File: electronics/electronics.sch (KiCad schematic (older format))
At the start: 19 parts, among them J3 EXTERNAL CONTROL, J4 POWER, J5 I2C BUS, J6 I2C BUS, J7 INPUT, J8 OUTPUT, U1 ProMicro

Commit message: Last through hole
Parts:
- R5, R6, R7, R8: footprint Resistor_THT:R_Axial_DIN0204_L3.6mm_D1.6mm_P1.90mm_Vertical -> Resistor_THT:R_Axial_DIN0204_L3.6mm_D1.6mm_P2.54mm_Vertical
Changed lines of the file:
@@
 F 0 "R5" H 7068 2346 50  0000 L CNN
 F 1 "75" H 7068 2255 50  0000 L CNN
-F 2 "Resistor_THT:R_Axial_DIN0204_L3.6mm_D1.6mm_P1.90mm_Vertical" H 7000 2300 50  0001 C CNN
+F 2 "Resistor_THT:R_Axial_DIN0204_L3.6mm_D1.6mm_P2.54mm_Vertical" H 7000 2300 50  0001 C CNN
 F 3 "~" H 7000 2300 50  0001 C CNN
 	1    7000 2300
@@
 F 0 "R6" H 7418 2346 50  0000 L CNN
 F 1 "75" H 7418 2255 50  0000 L CNN
-F 2 "Resistor_THT:R_Axial_DIN0204_L3.6mm_D1.6mm_P1.90mm_Vertical" H 7350 2300 50  0001 C CNN
+F 2 "Resistor_THT:R_Axial_DIN0204_L3.6mm_D1.6mm_P2.54mm_Vertical" H 7350 2300 50  0001 C CNN
 F 3 "~" H 7350 2300 50  0001 C CNN
 	1    7350 2300
@@
 F 0 "R7" H 7768 2346 50  0000 L CNN
 F 1 "75" H 7768 2255 50  0000 L CNN
-F 2 "Resistor_THT:R_Axial_DIN0204_L3.6mm_D1.6mm_P1.90mm_Vertical" H 7700 2300 50  0001 C CNN
+F 2 "Resistor_THT:R_Axial_DIN0204_L3.6mm_D1.6mm_P2.54mm_Vertical" H 7700 2300 50  0001 C CNN
 F 3 "~" H 7700 2300 50  0001 C CNN
 	1    7700 2300
@@
 F 0 "R8" H 8068 2346 50  0000 L CNN
 F 1 "75" H 8068 2255 50  0000 L CNN
-F 2 "Resistor_THT:R_Axial_DIN0204_L3.6mm_D1.6mm_P1.90mm_Vertical" H 8000 2300 50  0001 C CNN
+F 2 "Resistor_THT:R_Axial_DIN0204_L3.6mm_D1.6mm_P2.54mm_Vertical" H 8000 2300 50  0001 C CNN
 F 3 "~" H 8000 2300 50  0001 C CNN
 	1    8000 2300

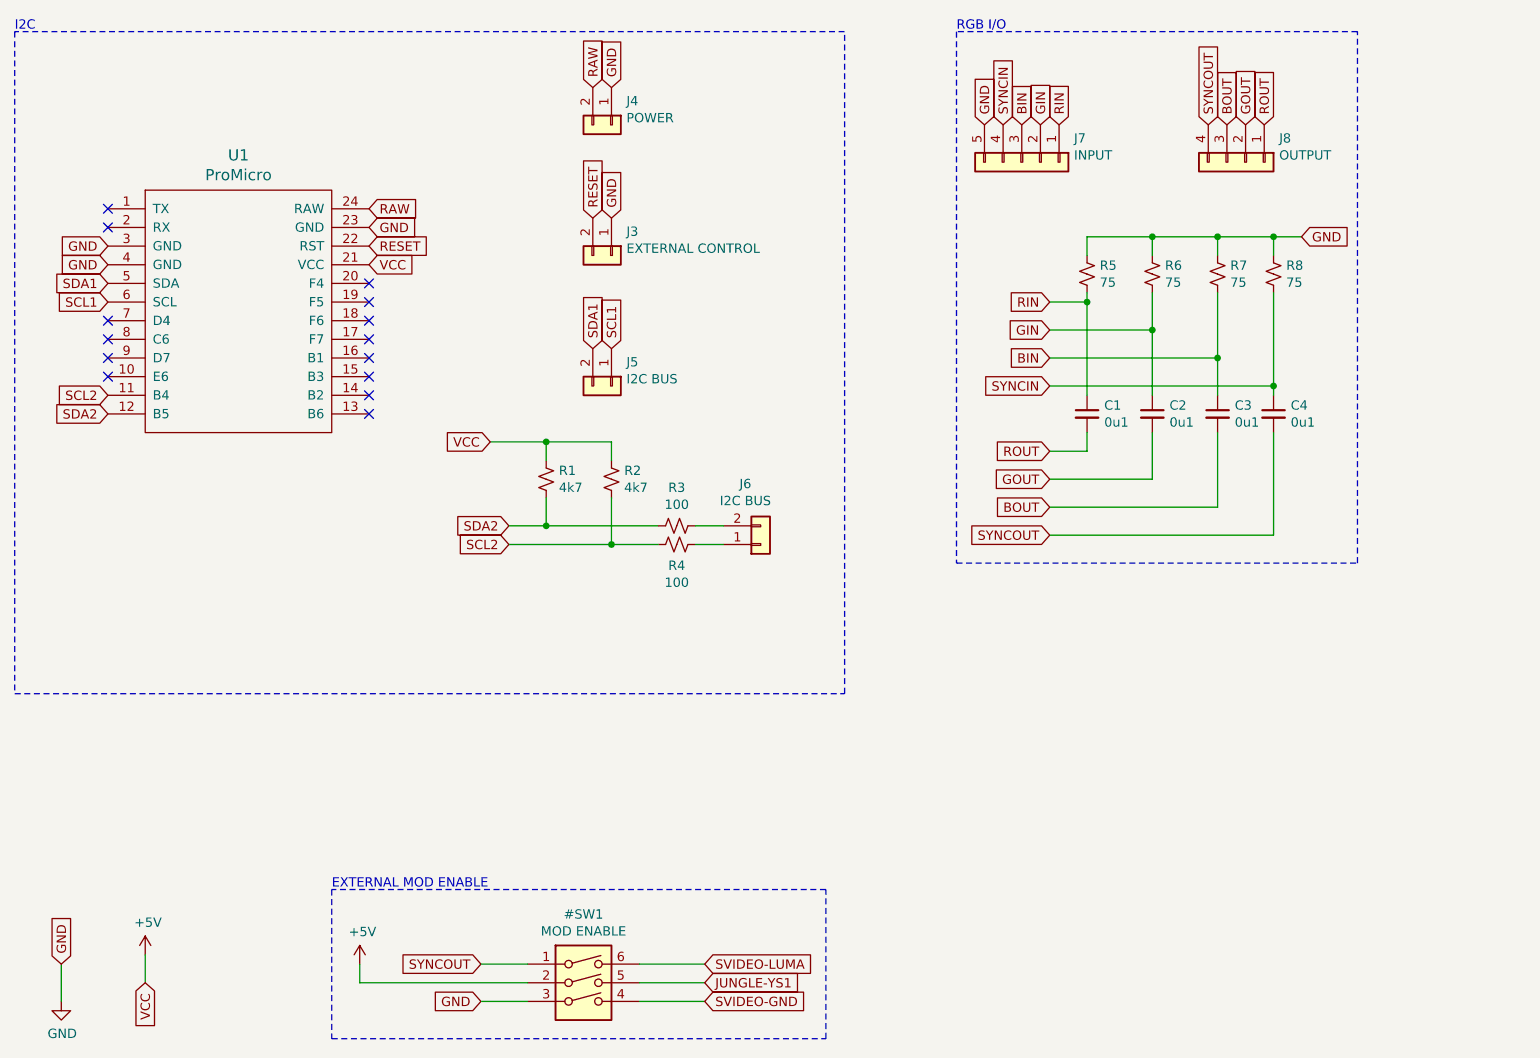
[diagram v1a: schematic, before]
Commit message: Encoder support
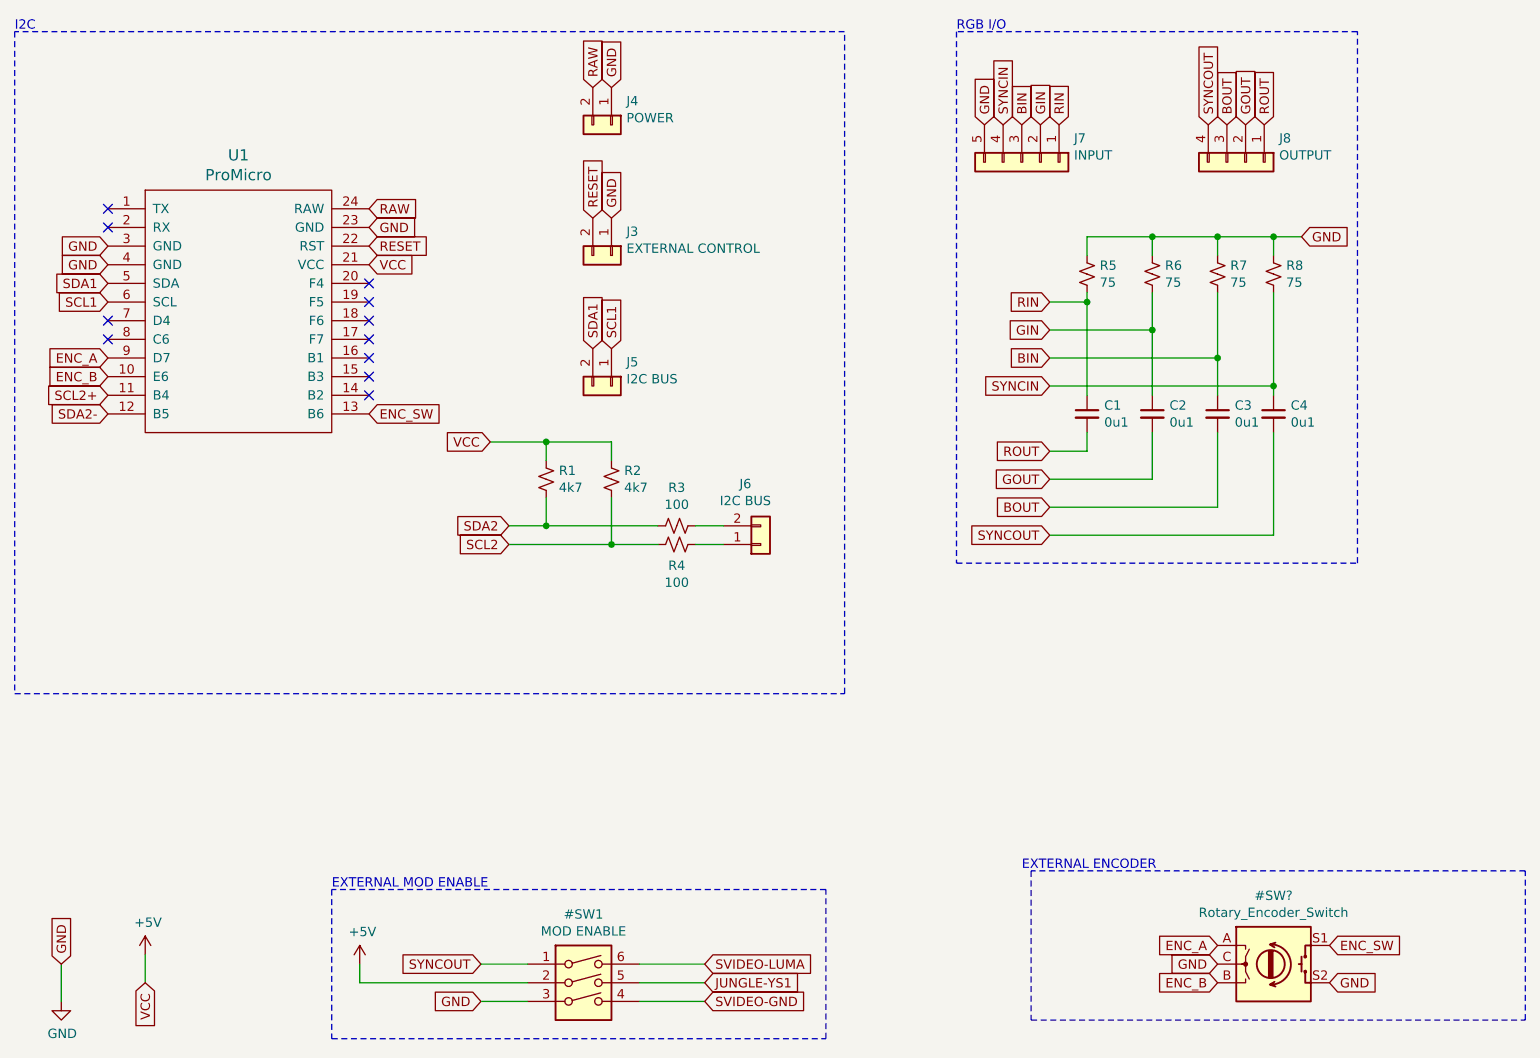
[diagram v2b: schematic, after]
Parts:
- C1, C2, C3, C4: footprint Capacitor_THT:C_Disc_D5.1mm_W3.2mm_P5.00mm -> Capacitor_SMD:C_0805_2012Metric_Pad1.18x1.45mm_HandSolder; Digikey PN (none) -> 478-10836-1-ND
- R1, R2: footprint Resistor_THT:R_Axial_DIN0207_L6.3mm_D2.5mm_P2.54mm_Vertical -> Resistor_SMD:R_0805_2012Metric_Pad1.20x1.40mm_HandSolder; Digikey PN (none) -> RMCF0805FT4K70CT-ND
- R3, R4: footprint Resistor_THT:R_Axial_DIN0207_L6.3mm_D2.5mm_P2.54mm_Vertical -> Resistor_SMD:R_0805_2012Metric_Pad1.20x1.40mm_HandSolder; Digikey PN (none) -> RMCF0805FT100RCT-ND
- R5, R6, R7, R8: footprint Resistor_THT:R_Axial_DIN0204_L3.6mm_D1.6mm_P2.54mm_Vertical -> Resistor_SMD:R_0805_2012Metric_Pad1.20x1.40mm_HandSolder; Digikey PN (none) -> RMCF0805FT75R0CT-ND
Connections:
- net SCL2: no longer U1.11 (B4)
- net SDA2: no longer U1.12 (B5)
- net ENC_B: now reaches U1.10 (E6)
- net ENC_SW: now reaches U1.13 (B6)
- net ENC_A: now reaches U1.9 (D7)
- new net SCL2+: U1.11 (B4)
- new net SDA2-: U1.12 (B5)
- no-connect marks 14 -> 11
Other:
- note added: "EXTERNAL ENCODER"
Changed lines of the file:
@@
 VCC
 Text GLabel 1750 2950 0    50   Input ~ 0
-SCL2
+SCL2+
 Text GLabel 1750 3050 0    50   Input ~ 0
-SDA2
+SDA2-
 Text GLabel 1750 2350 0    50   Input ~ 0
 SDA1
@@
 NoConn ~ 1750 2550
 NoConn ~ 1750 2650
-NoConn ~ 1750 2750
-NoConn ~ 1750 2850
 NoConn ~ 3150 2350
 NoConn ~ 3150 2450
@@
 NoConn ~ 3150 2850
 NoConn ~ 3150 2950
-NoConn ~ 3150 3050
 $Comp
 L Connector_Generic:Conn_01x05 J7
@@
 F 0 "R5" H 7068 2346 50  0000 L CNN
 F 1 "75" H 7068 2255 50  0000 L CNN
-F 2 "Resistor_THT:R_Axial_DIN0204_L3.6mm_D1.6mm_P2.54mm_Vertical" H 7000 2300 50  0001 C CNN
+F 2 "Resistor_SMD:R_0805_2012Metric_Pad1.20x1.40mm_HandSolder" H 7000 2300 50  0001 C CNN
 F 3 "~" H 7000 2300 50  0001 C CNN
+F 4 "RMCF0805FT75R0CT-ND " H 7000 2300 50  0001 C CNN "Digikey PN"
 	1    7000 2300
-	1    0    0    -1
-$EndComp
-$Comp
-L Device:R_Small_US R6
-U 1 1 6113D219
-P 7350 2300
-F 0 "R6" H 7418 2346 50  0000 L CNN
-F 1 "75" H 7418 2255 50  0000 L CNN
-F 2 "Resistor_THT:R_Axial_DIN0204_L3.6mm_D1.6mm_P2.54mm_Vertical" H 7350 2300 50  0001 C CNN
-F 3 "~" H 7350 2300 50  0001 C CNN
-	1    7350 2300
-	1    0    0    -1
-$EndComp
-$Comp
-L Device:R_Small_US R7
-U 1 1 6113D54B
-P 7700 2300
-F 0 "R7" H 7768 2346 50  0000 L CNN
-F 1 "75" H 7768 2255 50  0000 L CNN
-F 2 "Resistor_THT:R_Axial_DIN0204_L3.6mm_D1.6mm_P2.54mm_Vertical" H 7700 2300 50  0001 C CNN
-F 3 "~" H 7700 2300 50  0001 C CNN
-	1    7700 2300
-	1    0    0    -1
-$EndComp
-$Comp
-L Device:R_Small_US R8
-U 1 1 6113D855
-P 8000 2300
-F 0 "R8" H 8068 2346 50  0000 L CNN
-F 1 "75" H 8068 2255 50  0000 L CNN
-F 2 "Resistor_THT:R_Axial_DIN0204_L3.6mm_D1.6mm_P2.54mm_Vertical" H 8000 2300 50  0001 C CNN
-F 3 "~" H 8000 2300 50  0001 C CNN
-	1    8000 2300
 	1    0    0    -1
 $EndComp
@@
 F 0 "C1" H 7092 3096 50  0000 L CNN
 F 1 "0u1" H 7092 3005 50  0000 L CNN
-F 2 "Capacitor_THT:C_Disc_D5.1mm_W3.2mm_P5.00mm" H 7000 3050 50  0001 C CNN
+F 2 "Capacitor_SMD:C_0805_2012Metric_Pad1.18x1.45mm_HandSolder" H 7000 3050 50  0001 C CNN
 F 3 "~" H 7000 3050 50  0001 C CNN
+F 4 "478-10836-1-ND" H 7000 3050 50  0001 C CNN "Digikey PN"
 	1    7000 3050
-	1    0    0    -1
-$EndComp
-$Comp
-L Device:C_Small C2
-U 1 1 6114371A
-P 7350 3050
-F 0 "C2" H 7442 3096 50  0000 L CNN
-F 1 "0u1" H 7442 3005 50  0000 L CNN
-F 2 "Capacitor_THT:C_Disc_D5.1mm_W3.2mm_P5.00mm" H 7350 3050 50  0001 C CNN
-F 3 "~" H 7350 3050 50  0001 C CNN
-	1    7350 3050
-	1    0    0    -1
-$EndComp
-$Comp
-L Device:C_Small C3
-U 1 1 61143B2D
-P 7700 3050
-F 0 "C3" H 7792 3096 50  0000 L CNN
-F 1 "0u1" H 7792 3005 50  0000 L CNN
-F 2 "Capacitor_THT:C_Disc_D5.1mm_W3.2mm_P5.00mm" H 7700 3050 50  0001 C CNN
-F 3 "~" H 7700 3050 50  0001 C CNN
-	1    7700 3050
 	1    0    0    -1
 $EndComp
@@
 Wire Wire Line
 	7350 2100 7700 2100
-$Comp
-L Device:C_Small C4
-U 1 1 61143F72
-P 8000 3050
-F 0 "C4" H 8092 3096 50  0000 L CNN
-F 1 "0u1" H 8092 3005 50  0000 L CNN
-F 2 "Capacitor_THT:C_Disc_D5.1mm_W3.2mm_P5.00mm" H 8000 3050 50  0001 C CNN
-F 3 "~" H 8000 3050 50  0001 C CNN
-	1    8000 3050
-	1    0    0    -1
-$EndComp
 Wire Wire Line
 	8000 2400 8000 2900
@@
 F 0 "R1" H 4168 3446 50  0000 L CNN
 F 1 "4k7" H 4168 3355 50  0000 L CNN
-F 2 "Resistor_THT:R_Axial_DIN0207_L6.3mm_D2.5mm_P2.54mm_Vertical" H 4100 3400 50  0001 C CNN
+F 2 "Resistor_SMD:R_0805_2012Metric_Pad1.20x1.40mm_HandSolder" H 4100 3400 50  0001 C CNN
 F 3 "~" H 4100 3400 50  0001 C CNN
+F 4 "RMCF0805FT4K70CT-ND " H 4100 3400 50  0001 C CNN "Digikey PN"
 	1    4100 3400
-	1    0    0    -1
-$EndComp
-$Comp
-L Device:R_Small_US R2
-U 1 1 611740AA
-P 4450 3400
-F 0 "R2" H 4518 3446 50  0000 L CNN
-F 1 "4k7" H 4518 3355 50  0000 L CNN
-F 2 "Resistor_THT:R_Axial_DIN0207_L6.3mm_D2.5mm_P2.54mm_Vertical" H 4450 3400 50  0001 C CNN
-F 3 "~" H 4450 3400 50  0001 C CNN
-	1    4450 3400
 	1    0    0    -1
 $EndComp
@@
 F 0 "R3" V 4595 3650 50  0000 C CNN
 F 1 "100" V 4686 3650 50  0000 C CNN
-F 2 "Resistor_THT:R_Axial_DIN0207_L6.3mm_D2.5mm_P2.54mm_Vertical" H 4800 3650 50  0001 C CNN
+F 2 "Resistor_SMD:R_0805_2012Metric_Pad1.20x1.40mm_HandSolder" H 4800 3650 50  0001 C CNN
 F 3 "~" H 4800 3650 50  0001 C CNN
+F 4 "RMCF0805FT100RCT-ND " V 4800 3650 50  0001 C CNN "Digikey PN"
 	1    4800 3650
-	0    1    1    0
-$EndComp
-$Comp
-L Device:R_Small_US R4
-U 1 1 61177C29
-P 4800 3750
-F 0 "R4" V 4913 3750 50  0000 C CNN
-F 1 "100" V 5004 3750 50  0000 C CNN
-F 2 "Resistor_THT:R_Axial_DIN0207_L6.3mm_D2.5mm_P2.54mm_Vertical" H 4800 3750 50  0001 C CNN
-F 3 "~" H 4800 3750 50  0001 C CNN
-	1    4800 3750
 	0    1    1    0
 $EndComp
@@
 Text Notes 2950 5600 0    50   ~ 0
 EXTERNAL MOD ENABLE
+$Comp
+L Device:R_Small_US R2
+U 1 1 6128C924
+P 4450 3400
+F 0 "R2" H 4518 3446 50  0000 L CNN
+F 1 "4k7" H 4518 3355 50  0000 L CNN
+F 2 "Resistor_SMD:R_0805_2012Metric_Pad1.20x1.40mm_HandSolder" H 4450 3400 50  0001 C CNN
+F 3 "~" H 4450 3400 50  0001 C CNN
+F 4 "RMCF0805FT4K70CT-ND " H 4450 3400 50  0001 C CNN "Digikey PN"
+	1    4450 3400
+	1    0    0    -1
+$EndComp
+$Comp
+L Device:R_Small_US R4
+U 1 1 6128CD81
+P 4800 3750
+F 0 "R4" V 4913 3750 50  0000 C CNN
+F 1 "100" V 5004 3750 50  0000 C CNN
+F 2 "Resistor_SMD:R_0805_2012Metric_Pad1.20x1.40mm_HandSolder" H 4800 3750 50  0001 C CNN
+F 3 "~" H 4800 3750 50  0001 C CNN
+F 4 "RMCF0805FT100RCT-ND " V 4800 3750 50  0001 C CNN "Digikey PN"
+	1    4800 3750
+	0    1    1    0
+$EndComp
+$Comp
+L Device:R_Small_US R6
+U 1 1 6128D0EC
+P 7350 2300
+F 0 "R6" H 7418 2346 50  0000 L CNN
+F 1 "75" H 7418 2255 50  0000 L CNN
+F 2 "Resistor_SMD:R_0805_2012Metric_Pad1.20x1.40mm_HandSolder" H 7350 2300 50  0001 C CNN
+F 3 "~" H 7350 2300 50  0001 C CNN
+F 4 "" H 7350 2300 50  0001 C CNN "Digkey PN"
+F 5 "RMCF0805FT75R0CT-ND " H 7350 2300 50  0001 C CNN "Digikey PN"
+	1    7350 2300
+	1    0    0    -1
+$EndComp
+$Comp
+L Device:R_Small_US R7
+U 1 1 6128F8BC
+P 7700 2300
+F 0 "R7" H 7768 2346 50  0000 L CNN
+F 1 "75" H 7768 2255 50  0000 L CNN
+F 2 "Resistor_SMD:R_0805_2012Metric_Pad1.20x1.40mm_HandSolder" H 7700 2300 50  0001 C CNN
+F 3 "~" H 7700 2300 50  0001 C CNN
+F 4 "" H 7700 2300 50  0001 C CNN "Digkey PN"
+F 5 "RMCF0805FT75R0CT-ND " H 7700 2300 50  0001 C CNN "Digikey PN"
+	1    7700 2300
+	1    0    0    -1
+$EndComp
+$Comp
+L Device:R_Small_US R8
+U 1 1 6128FBDD
+P 8000 2300
+F 0 "R8" H 8068 2346 50  0000 L CNN
+F 1 "75" H 8068 2255 50  0000 L CNN
+F 2 "Resistor_SMD:R_0805_2012Metric_Pad1.20x1.40mm_HandSolder" H 8000 2300 50  0001 C CNN
+F 3 "~" H 8000 2300 50  0001 C CNN
+F 4 "" H 8000 2300 50  0001 C CNN "Digkey PN"
+F 5 "RMCF0805FT75R0CT-ND " H 8000 2300 50  0001 C CNN "Digikey PN"
+	1    8000 2300
+	1    0    0    -1
+$EndComp
+$Comp
+L Device:C_Small C2
+U 1 1 61292639
+P 7350 3050
+F 0 "C2" H 7442 3096 50  0000 L CNN
+F 1 "0u1" H 7442 3005 50  0000 L CNN
+F 2 "Capacitor_SMD:C_0805_2012Metric_Pad1.18x1.45mm_HandSolder" H 7350 3050 50  0001 C CNN
+F 3 "~" H 7350 3050 50  0001 C CNN
+F 4 "478-10836-1-ND" H 7350 3050 50  0001 C CNN "Digikey PN"
+	1    7350 3050
+	1    0    0    -1
+$EndComp
+$Comp
+L Device:C_Small C3
+U 1 1 61292960
+P 7700 3050
+F 0 "C3" H 7792 3096 50  0000 L CNN
+F 1 "0u1" H 7792 3005 50  0000 L CNN
+F 2 "Capacitor_SMD:C_0805_2012Metric_Pad1.18x1.45mm_HandSolder" H 7700 3050 50  0001 C CNN
+F 3 "~" H 7700 3050 50  0001 C CNN
+F 4 "478-10836-1-ND" H 7700 3050 50  0001 C CNN "Digikey PN"
+	1    7700 3050
+	1    0    0    -1
+$EndComp
+$Comp
+L Device:C_Small C4
+U 1 1 61292C9D
+P 8000 3050
+F 0 "C4" H 8092 3096 50  0000 L CNN
+F 1 "0u1" H 8092 3005 50  0000 L CNN
+F 2 "Capacitor_SMD:C_0805_2012Metric_Pad1.18x1.45mm_HandSolder" H 8000 3050 50  0001 C CNN
+F 3 "~" H 8000 3050 50  0001 C CNN
+F 4 "478-10836-1-ND" H 8000 3050 50  0001 C CNN "Digikey PN"
+	1    8000 3050
+	1    0    0    -1
+$EndComp
+$Comp
+L Device:Rotary_Encoder_Switch #SW?
+U 1 1 612F1AAA
+P 8000 6000
+F 0 "#SW?" H 8000 6367 50  0000 C CNN
+F 1 "Rotary_Encoder_Switch" H 8000 6276 50  0000 C CNN
+F 2 "" H 7850 6160 50  0001 C CNN
+F 3 "~" H 8000 6260 50  0001 C CNN
+	1    8000 6000
+	1    0    0    -1
+$EndComp
+Wire Notes Line
+	9350 6300 9350 5500
+Wire Notes Line
+	9350 5500 6700 5500
+Wire Notes Line
+	6700 5500 6700 6300
+Wire Notes Line
+	6700 6300 9350 6300
+Text Notes 6650 5500 0    50   ~ 0
+EXTERNAL ENCODER
+Text GLabel 7700 6000 0    50   Input ~ 0
+GND
+Text GLabel 8300 6100 2    50   Input ~ 0
+GND
+Text GLabel 7700 5900 0    50   Input ~ 0
+ENC_A
+Text GLabel 7700 6100 0    50   Input ~ 0
+ENC_B
+Text GLabel 8300 5900 2    50   Input ~ 0
+ENC_SW
+Text GLabel 3150 3050 2    50   Input ~ 0
+ENC_SW
+Text GLabel 1750 2750 0    50   Input ~ 0
+ENC_A
+Text GLabel 1750 2850 0    50   Input ~ 0
+ENC_B
 $EndSCHEMATC
